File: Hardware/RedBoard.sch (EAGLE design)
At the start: 54 parts, among them IC1 FT232RLSSOP, IC2 LMV358, IC3 LM1117, J1 ICSP, J4 POWER_JACKSMD, Q1 MOSFET-PCHANNELSMD, U2 MIC5205, U3 ATMEGA328, Y1 16MHz

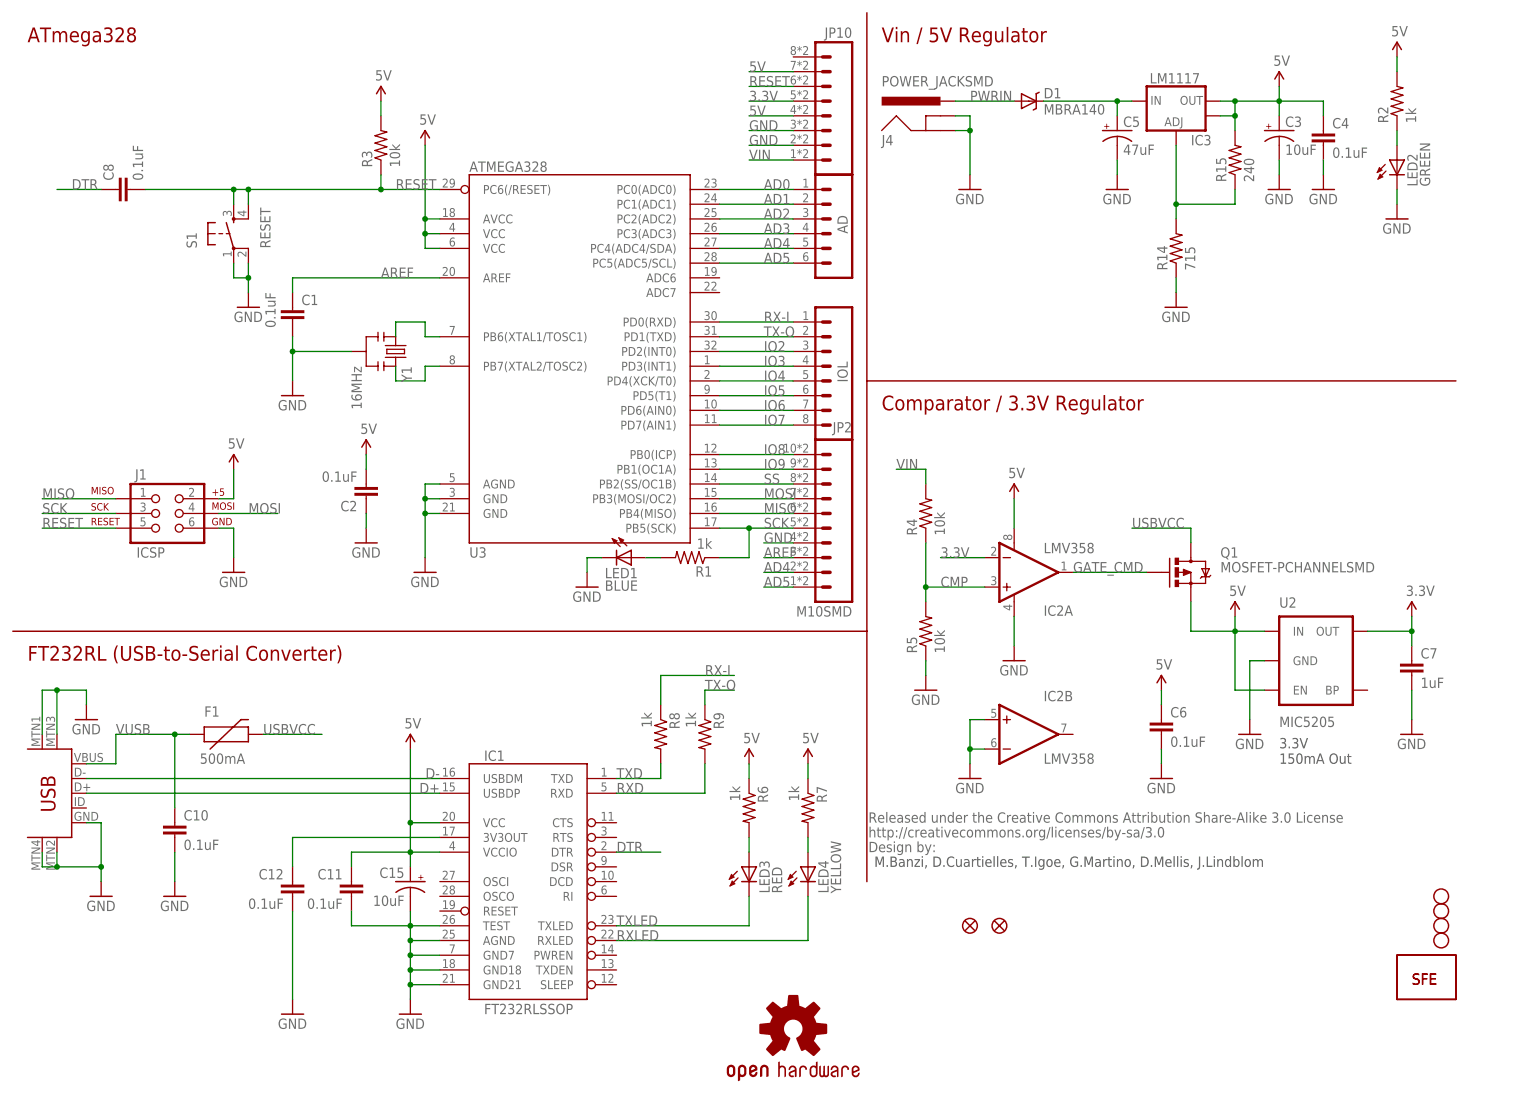
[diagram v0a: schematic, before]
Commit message: New SMD ICSP header, logo, FT231X, power select
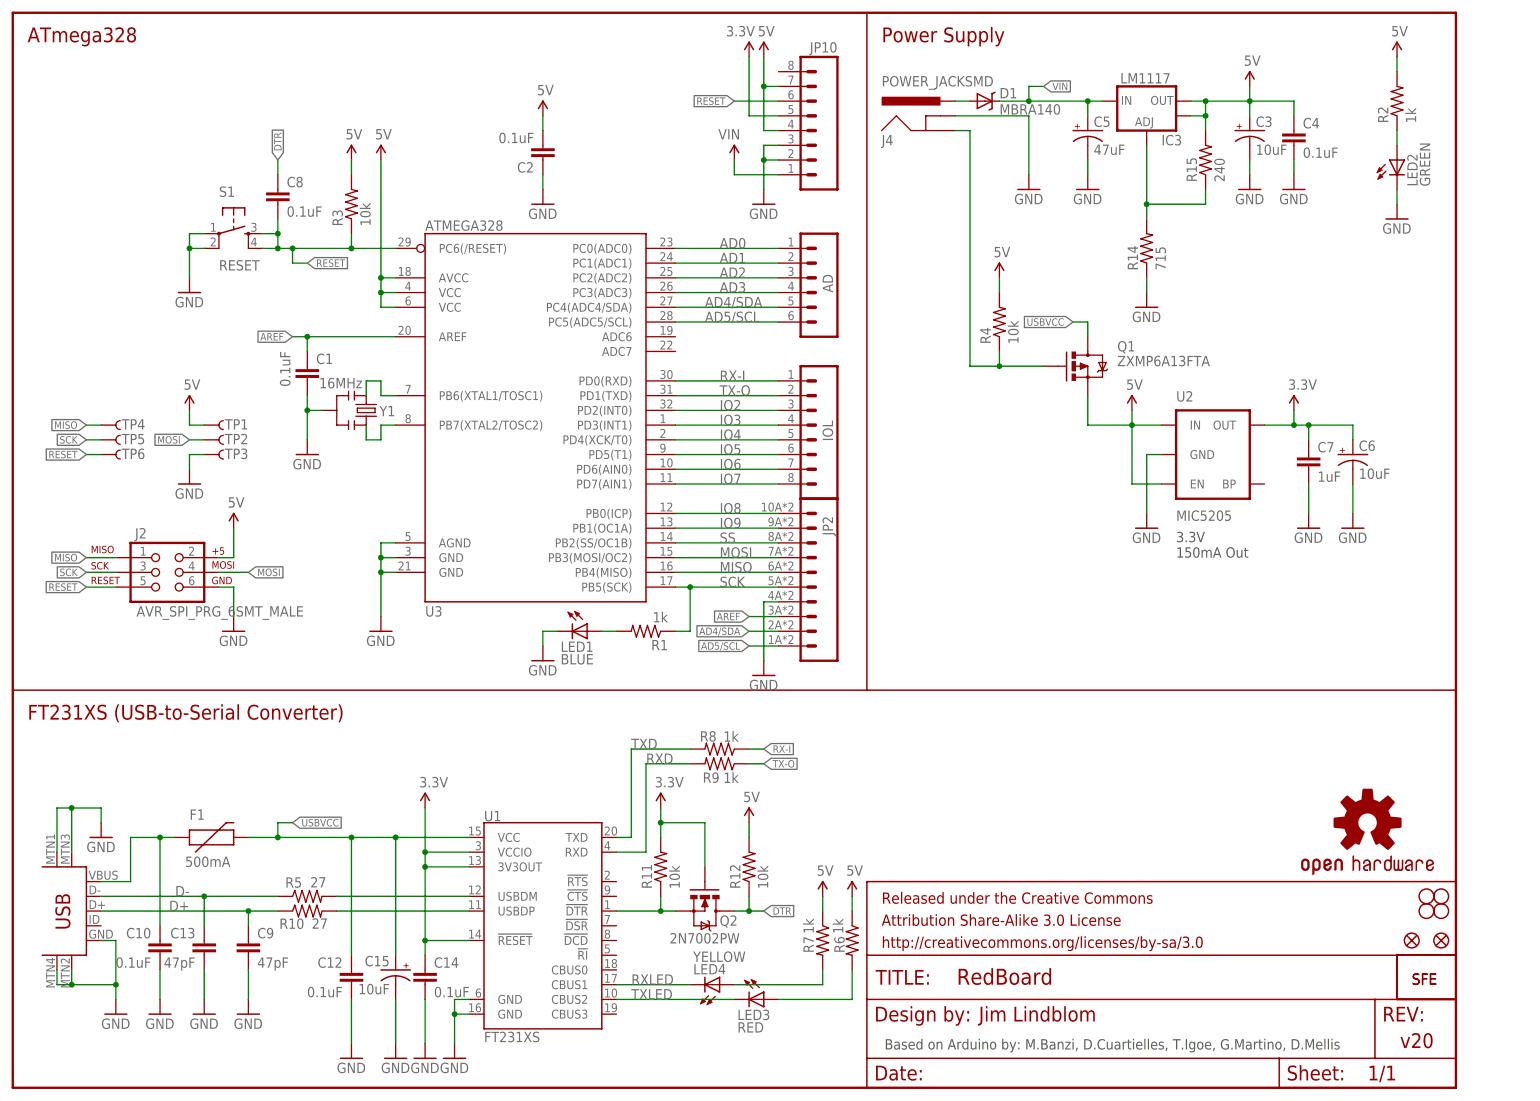
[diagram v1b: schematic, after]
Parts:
- removed C11: 0.1uF, SparkFun-Capacitors:CAP0402-CAP
- removed IC1: FT232RLSSOP, SparkFun-DigitalIC:FT232RLSSOP
- removed IC2: LMV358, SparkFun:OPAMP-DUALU
- removed J1: ICSP, SparkFun:AVR_SPI_PRG_6PTH
- removed U$15: CREATIVE_COMMONS, SparkFun:CREATIVE_COMMONS
- added C13, C9: 47pF, SparkFun-Capacitors:47PF-50V-5%(0603)
- added C14: 0.1uF, SparkFun:CAP0603-CAP
- added FRAME2: FRAME-LETTER, SparkFun-Aesthetics:FRAME-LETTER
- added J2: AVR_SPI_PRG_6SMT_MALE, SparkFun-Connectors:AVR_SPI_PRG_6SMT_MALE
- added Q2: 2N7002PW, SparkFun-DiscreteSemi:MOSFET-NCHANNEL2N7002PW
- added R10: 27, SparkFun-Resistors:RESISTOR0603-RES
- added R11, R12: 10k, SparkFun:RESISTOR0603-RES
- added TP1, TP2, TP3, TP4, TP5, TP6: TP-3x5, SparkFun-Passives:TEST-POINT3X5
- added U1: FT231XS, SparkFun-DigitalIC:FT231XS
- C1, C10, C12, C2, C4, C7, C8: device SparkFun:CAP0402-CAP -> SparkFun:CAP0603-CAP
- C6: value 0.1uF -> 10uF; device SparkFun:CAP0402-CAP -> SparkFun:CAP_POL1206
- JP2: value M10SMD -> M10SMD_COMBO; device SparkFun-Connectors:M10SMD -> SparkFun-Connectors:M10SMD_COMBO
- Q1: value MOSFET-PCHANNELSMD -> ZXMP6A13FTA
- R1, R14, R15, R2, R3, R4, R6, R7, R8, R9: device SparkFun:RESISTOR0402-RES -> SparkFun:RESISTOR0603-RES
- R5: value 10k -> 27; device SparkFun:RESISTOR0402-RES -> SparkFun-Resistors:RESISTOR0603-RES
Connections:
- net AD4 renamed AD4/SDA
- net AD5 renamed AD5/SCL
- removed net CMP: IC2A.+IN, R4.1, R5.2
- removed net GATE_CMD: IC2A.OUT, Q1.G
- removed net N$5: C12.1, IC1.3V3OUT
- new net INSERT: J4.GND, Q1.G, R4.1
- new net N$12: Q2.S, R11.1, U1.!DTR
- new net N$6: R5.2, U1.USBDM
- new net N$7: R10.2, U1.USBDP
- net 3.3V: now also C14.1, C6.+, Q2.G, R11.2, U1.!RESET, U1.3V3OUT, U1.VCCIO; no longer IC2A.-IN
- net 5V: now also J2.2, R12.2, R4.2, TP1.1; no longer C11.1, C15.+, C6.1, IC1.VCC, IC1.VCCIO, IC2A.V+, J1.2
- net D+: now also C9.1, R10.1; no longer IC1.USBDP
- net D-: now also C13.1, R5.1; no longer IC1.USBDM
- net DTR: now also Q2.D, R12.1; no longer IC1.DTR
- net GND: now also C13.2, C14.2, C6.-, C9.2, J2.6, TP3.1, U1.GND@16, U1.GND@6; no longer C11.2, C6.2, IC1.AGND, IC1.GND18, IC1.GND21, IC1.GND7, IC1.TEST, IC2A.V-, IC2B.+IN, IC2B.-IN, J1.6, J4.GND, R5.1
- net MISO: now also J2.1, TP4.1; no longer J1.1
- net MOSI: now also J2.4, TP2.1; no longer J1.4
- net RESET: now also J2.5, TP6.1; no longer J1.5
- net RXD: now also U1.RXD; no longer IC1.RXD
- net RXLED: now also U1.CBUS1; no longer IC1.RXLED
- net SCK: now also J2.3, TP5.1; no longer J1.3
- net TXD: now also U1.TXD; no longer IC1.TXD
- net TXLED: now also U1.CBUS2; no longer IC1.TXLED
- net USBVCC: now also C12.1, C15.+, U1.VCC
- net VIN: no longer R4.2
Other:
- note added: "Based on Arduino by: M.Banzi, D.Cuartielles, T.Igoe, G.Martino, D.Mellis"
- note added: "FT231XS (USB-to-Serial Converter)"
- note added: "Jim Lindblom"
- note added: "Power Supply"
- note added: "v20"
- note removed: "Comparator / 3.3V Regulator"
- note removed: "FT232RL (USB-to-Serial Converter)"
- note removed: "M.Banzi, D.Cuartielles, T.Igoe, G.Martino, D.Mellis, J.Lindblom"
- note removed: "Vin / 5V Regulator"
- moved on the sheet: AD, C1, C10, C12, C15, C2, C3, C4, C5, C7, C8, D1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

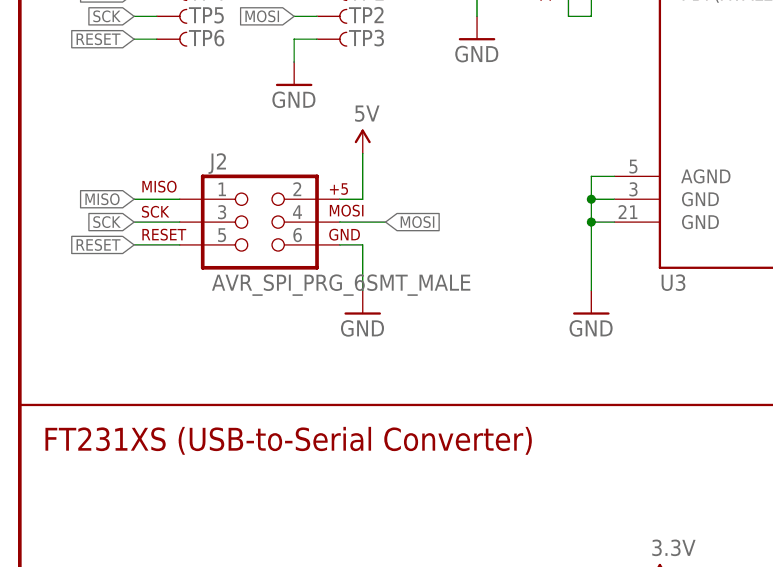
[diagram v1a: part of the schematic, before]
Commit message: Switch RX/TX labels, updating back logo
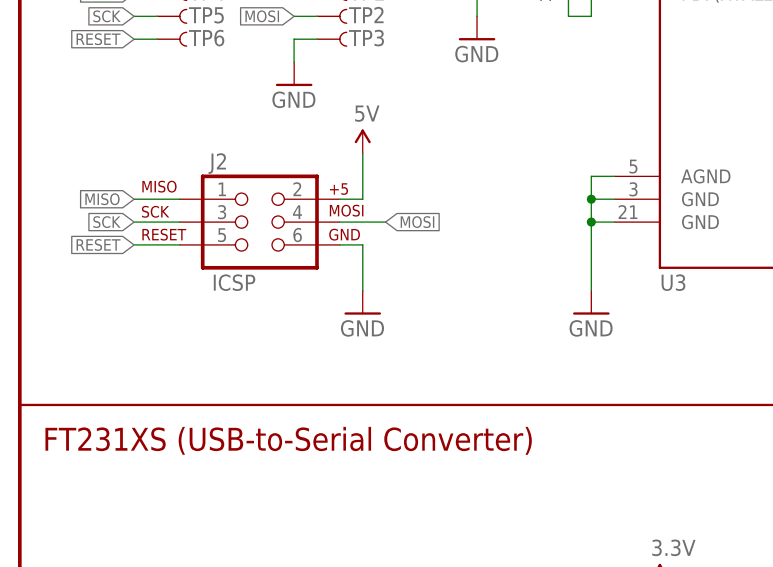
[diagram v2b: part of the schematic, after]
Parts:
- J2: value AVR_SPI_PRG_6SMT_MALE -> ICSP
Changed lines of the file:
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@@
 <part name="JP1" library="SparkFun-Aesthetics" deviceset="LOGO-SFE" device="NW2"/>
 <part name="JP7" library="SparkFun-Aesthetics" deviceset="LOGO-SFE" device="SK"/>
-<part name="J2" library="SparkFun-Connectors" deviceset="AVR_SPI_PRG_6" device="SMT_MALE"/>
+<part name="J2" library="SparkFun-Connectors" deviceset="AVR_SPI_PRG_6" device="SMT_MALE" value="ICSP"/>
 <part name="C6" library="SparkFun" deviceset="CAP_POL" device="1206" value="10uF"/>
 <part name="GND14" library="SparkFun" deviceset="GND" device=""/>

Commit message: LEDs to 1206; new barrel jack fp; moved 5V vreg
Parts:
- removed J4: POWER_JACKSMD, SparkFun:POWER_JACKSMD
- added J1: POWER_JACKOVERPASTE_REDBOARD_0603, Testing:POWER_JACKOVERPASTE_REDBOARD_0603
- LED1: value BLUE -> Blue; device SparkFun:LED0603 -> SparkFun-LED:LED1206-NS
- LED2: value GREEN -> Green; device SparkFun:LED0603 -> SparkFun-LED:LED1206-NS
- LED3: value RED -> Red; device SparkFun:LED0603 -> SparkFun-LED:LED1206-NS
- LED4: value YELLOW -> Yellow; device SparkFun:LED0603 -> SparkFun-LED:LED1206-NS
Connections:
- net GND: now also J1.GNDBREAK; no longer J4.GNDBREAK
- net INSERT: now also J1.GND; no longer J4.GND
- net PWRIN: now also J1.PWR; no longer J4.PWR
